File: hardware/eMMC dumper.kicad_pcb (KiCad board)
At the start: 2 copper layers, 85.8 x 55 mm, 49 parts, among them U1 F1C100s, U2 AMS1117-3.3, U3 TLV75512PDBV (WL9193S5-12), U4 EMMC04G-M627-A01

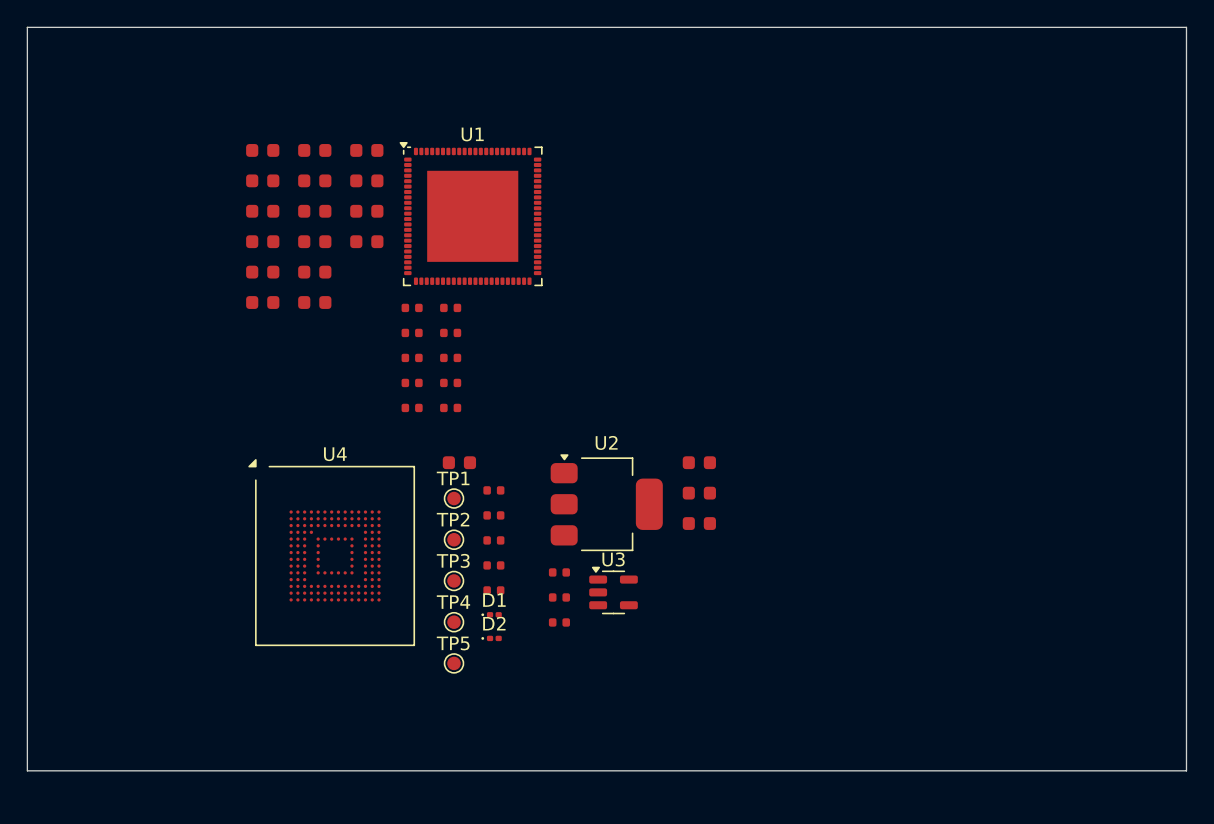
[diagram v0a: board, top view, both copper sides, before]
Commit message: Started placing decoupling capacitors
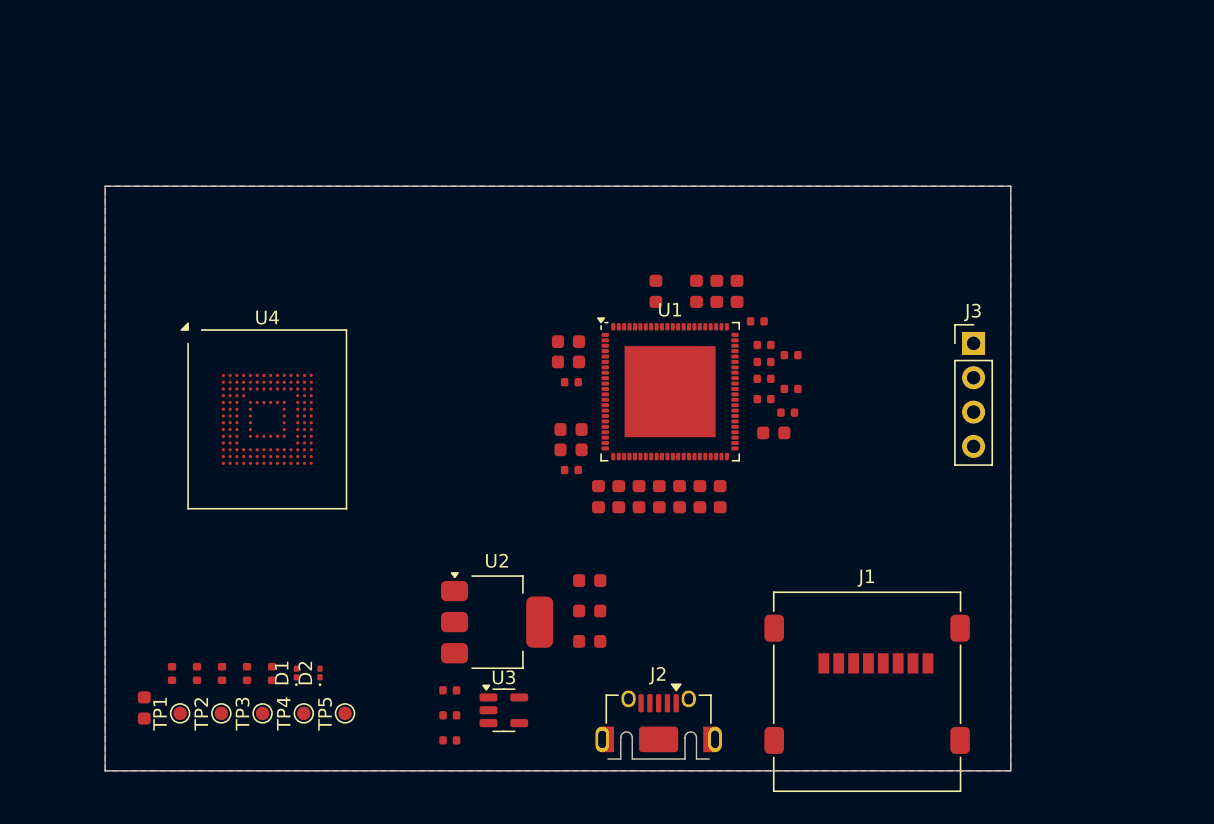
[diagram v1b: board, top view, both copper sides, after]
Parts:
- added J1: Micro_SD_Card, Connector_Card:microSD_HC_Molex_47219-2001, F.Cu at (182.1, 119.4)
- added J2: USB_B_Micro, Connector_USB:USB_Micro-AB_Molex_47590-0001, F.Cu at (166.7, 123.3)
- added J3: Conn_01x04, Connector_PinHeader_2.54mm:PinHeader_1x04_P2.54mm_Vertical, F.Cu at (190.0, 93.6)
- moved C9 39.9 mm to (169.8, 105.0), turned to -90 degrees
- moved C13 39.0 mm to (175.2, 100.2)
- moved C16 36.7 mm to (171.2, 105.0), turned to -90 degrees
- moved C11 35.3 mm to (172.5, 89.8), turned to 90 degrees
- moved C10 34.1 mm to (171.0, 89.8), turned to 90 degrees
- moved C18 32.9 mm to (168.2, 105.0), turned to -90 degrees
- moved C7 31.8 mm to (160.2, 101.5), turned to 180 degrees
- moved C19 30.4 mm to (166.8, 105.0), turned to -90 degrees
- moved C26 29.5 mm to (128.7, 120.6), turned to 90 degrees
- moved C23 28.2 mm to (163.8, 105.0), turned to -90 degrees
- moved R1 28.1 mm to (176.5, 94.5), turned to 180 degrees
- moved C24 27.6 mm to (165.2, 105.0), turned to -90 degrees
- moved R8 27.4 mm to (130.7, 118.0), turned to 90 degrees
- moved C14 27.3 mm to (166.5, 89.8), turned to 90 degrees
- moved C21 26.5 mm to (169.5, 89.8), turned to 90 degrees
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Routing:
- added copper zone on B.Cu, net GND
- added copper zone on F.Cu, net GND
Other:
- board size 85.8 x 55 mm -> 67 x 43.2 mm

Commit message: PCB major changes
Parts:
- removed J3: Conn_01x04, Connector_PinHeader_2.54mm:PinHeader_1x04_P2.54mm_Vertical
- added D3: LED, LED_SMD:LED_0201_0603Metric, F.Cu at (182.5, 93.6)
- added D4: LED, LED_SMD:LED_0201_0603Metric, F.Cu at (185.8, 93.6)
- added D5: LED, LED_SMD:LED_0201_0603Metric, F.Cu at (164.0, 116.4)
- added H1: MountingHole, MountingHole:MountingHole_3.2mm_M3, F.Cu at (128.8, 120.6)
- added H2: MountingHole, MountingHole:MountingHole_3.2mm_M3, F.Cu at (190.4, 95.8)
- added R13: 1kΩ, PCM_JLCPCB:R_0603, F.Cu at (177.0, 96.4)
- added R14: 1kΩ, PCM_JLCPCB:R_0603, F.Cu at (179.2, 96.4)
- added R15: 1kΩ, PCM_JLCPCB:R_0603, F.Cu at (181.5, 96.4)
- added R16: 1kΩ, PCM_JLCPCB:R_0603, F.Cu at (183.8, 96.4)
- added R17: 1kΩ, PCM_JLCPCB:R_0603, F.Cu at (160.2, 116.4)
- added TP6: TestPoint, TestPoint:TestPoint_Pad_D1.0mm, F.Cu at (149.2, 112.6)
- added TP7: TestPoint, TestPoint:TestPoint_Pad_D1.0mm, F.Cu at (153.4, 112.6)
- added TP8: TestPoint, TestPoint:TestPoint_Pad_D1.0mm, F.Cu at (157.8, 112.8)
- moved C26 54.8 mm to (182.6, 110.6), turned to 0 degrees
- moved D2 44.9 mm to (179.2, 93.5)
- moved TP1 44.5 mm to (171.2, 101.4)
- moved D1 43.5 mm to (175.8, 93.4)
- moved TP2 42.9 mm to (171.2, 99.0)
- moved TP3 41.8 mm to (171.2, 96.4)
- moved R8 39.8 mm to (170.1, 112.6), turned to 0 degrees
- moved R9 38.1 mm to (170.1, 111.6), turned to 0 degrees
- moved R10 36.5 mm to (170.1, 110.6), turned to 0 degrees
- moved R11 34.9 mm to (170.1, 109.6), turned to 0 degrees
- moved R12 33.4 mm to (170.1, 108.6), turned to 0 degrees
- moved C10 27.3 mm to (144.9, 97.8)
- moved C11 27.3 mm to (146.4, 97.8)
- moved C12 27.3 mm to (134.2, 108.0)
- moved C13 27.3 mm to (149.2, 108.3)
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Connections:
- D1 pad 2: /Linux_core/LED_GRN -> /Linux_core/LED_1
- D2 pad 2: /Linux_core/LED_RED -> /Linux_core/LED_2
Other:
- board size 67 x 43.2 mm -> 69.4 x 36 mm
- board text added: "0x01 init"
- board text added: "0x02 boot1"
- board text added: "0x03 boot2"
- board text added: "0x04 usrsp"
- board text added: "0x05 gmem"
- board text added: "0x06 bmem"
- board text added: "0x07 finish"
- board text added: "0x08 error"

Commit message: Moved LEDs, renamed testpoints
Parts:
- moved D4 58.9 mm to (126.9, 95.6), turned to -90 degrees
- moved R16 57.4 mm to (126.9, 104.3), turned to -90 degrees
- moved D3 53.8 mm to (128.7, 95.5), turned to -90 degrees
- moved R15 53.1 mm to (128.7, 102.3), turned to -90 degrees
- moved R14 49.0 mm to (130.4, 100.5), turned to -90 degrees
- moved D2 48.7 mm to (130.5, 95.5), turned to -90 degrees
- moved R13 44.6 mm to (132.5, 99.0), turned to -90 degrees
- moved D1 43.4 mm to (132.4, 95.5), turned to -90 degrees
- moved H2 24.5 mm to (190.1, 120.3)
- moved R12 10.8 mm to (180.8, 110.1)
- moved R11 9.95 mm to (179.9, 111.3)
- moved C26 7.77 mm to (186.0, 117.6), turned to 90 degrees
- moved R10 5.26 mm to (175.3, 111.4)
- moved J1 5.03 mm to (177.1, 119.5)
- moved R9 3.92 mm to (173.8, 110.3)
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- renumbered TP5 to 1V2, TP4 to 3V3, TP2 to CLK1, TP1 to CMD1, TP3 to D0, TP8 to GND1, TP7 to U_RX1, TP6 to U_TX1
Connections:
- R13 pad 2: unconnected-(R13-Pad2) -> Net-(U1A-PD0/LCD_D2/TWI0_SDA/RSB_SDA/EINTD0)
- R14 pad 2: unconnected-(R14-Pad2) -> Net-(U1A-PD1/LCD_D3/UART1_RTS/EINTD1)
- R15 pad 2: unconnected-(R15-Pad2) -> Net-(U1A-PD2/LCD_D4/UART1_CTS/EINTD2)
- R16 pad 2: unconnected-(R16-Pad2) -> Net-(U1A-PD3/LCD_D5/UART1_RX/EINTD3)
- U1 pad 6: unconnected-(U1A-PD0/LCD_D2/TWI0_SDA/RSB_SDA/EINTD0-Pad6) -> Net-(U1A-PD0/LCD_D2/TWI0_SDA/RSB_SDA/EINTD0)
- U1 pad 7: unconnected-(U1A-PD1/LCD_D3/UART1_RTS/EINTD1-Pad7) -> Net-(U1A-PD1/LCD_D3/UART1_RTS/EINTD1)
- U1 pad 8: unconnected-(U1A-PD2/LCD_D4/UART1_CTS/EINTD2-Pad8) -> Net-(U1A-PD2/LCD_D4/UART1_CTS/EINTD2)
- U1 pad 9: unconnected-(U1A-PD3/LCD_D5/UART1_RX/EINTD3-Pad9) -> Net-(U1A-PD3/LCD_D5/UART1_RX/EINTD3)
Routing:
- net +3V3: track 0.00 -> 11.8 mm
- net GND: track 0.00 -> 8.96 mm
- net /Linux_core/D3: track 0.00 -> 7.50 mm
- net /Linux_core/D1: track 0.00 -> 7.43 mm
- net /Linux_core/D2: track 0.00 -> 6.29 mm
- net /Linux_core/D0: track 0.00 -> 6.23 mm
- net /Linux_core/CMD: track 0.00 -> 6.12 mm

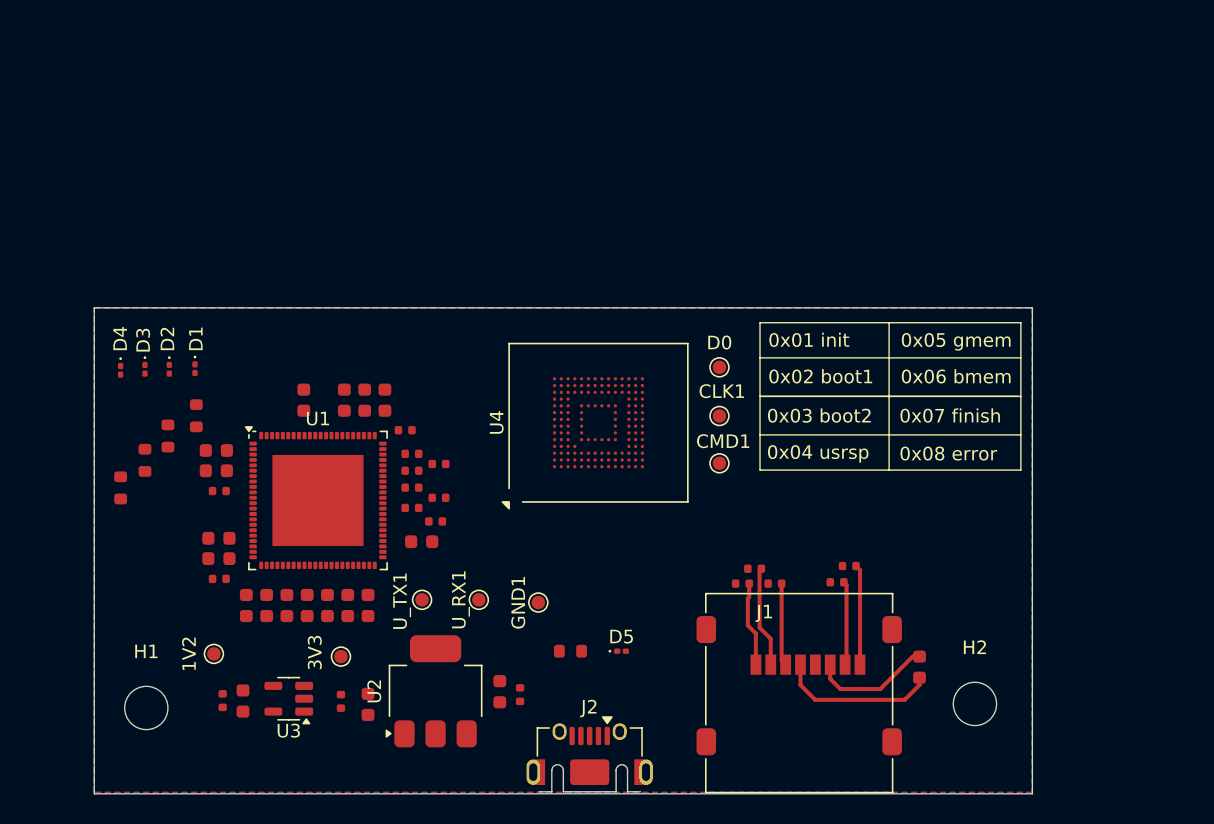
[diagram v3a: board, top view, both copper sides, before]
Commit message: Moved some parts, started routing
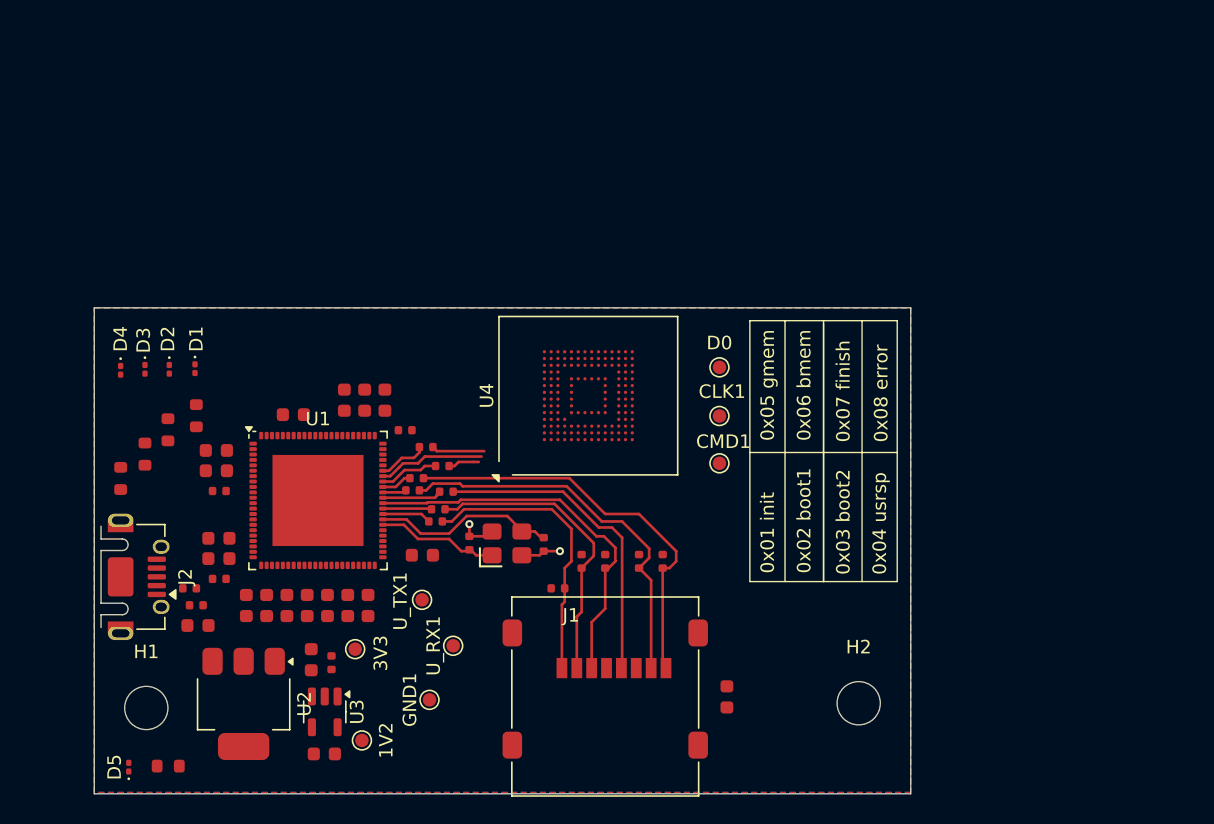
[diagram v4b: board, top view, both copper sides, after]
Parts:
- added C27: 18pF, PCM_JLCPCB:C_0402, F.Cu at (152.7, 108.4)
- added C28: 18pF, PCM_JLCPCB:C_0402, F.Cu at (158.2, 108.5)
- added X1: 24MHz, PCM_JLCPCB:OSC-SMD_4P-L3.2-W2.5-BL, F.Cu at (155.5, 108.4)
- moved J2 38.0 mm to (126.5, 110.9), turned to -90 degrees
- moved D5 37.5 mm to (127.5, 125.0), turned to 90 degrees
- moved R17 31.0 mm to (130.4, 124.9), turned to 0 degrees
- moved C5 24.8 mm to (132.5, 113.0), turned to 0 degrees
- moved C1 22.9 mm to (132.6, 114.5), turned to 0 degrees
- moved R11 14.7 mm to (165.2, 109.8), turned to -90 degrees
- moved C26 14.4 mm to (171.8, 119.8)
- moved J1 14.4 mm to (162.8, 119.8)
- moved U2 14.2 mm to (136.0, 120.3), turned to -90 degrees
- moved R12 13.8 mm to (167.0, 109.8), turned to -90 degrees
- moved R8 13.7 mm to (159.2, 111.8)
- moved R9 12.8 mm to (161.0, 109.8), turned to -90 degrees
- moved 1V2 12.7 mm to (144.8, 123.0), turned to -90 degrees
- moved R10 12.7 mm to (162.8, 109.8), turned to -90 degrees
- moved GND1 10.8 mm to (149.8, 120.0)
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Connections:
- U1 pad 51: unconnected-(U1A-HOSCI-Pad51) -> Net-(U1A-HOSCI)
- U1 pad 52: unconnected-(U1A-HOSCO-Pad52) -> Net-(U1A-HOSCO)
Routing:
- net /Linux_core/CLK: track 0.00 -> 23.6 mm
- net /Linux_core/D1: track 7.43 -> 30.4 mm
- net /Linux_core/D0: track 6.23 -> 28.7 mm
- net /Linux_core/CMD: track 6.12 -> 28.5 mm
- net /Linux_core/D2: track 6.29 -> 21.1 mm
- net /Linux_core/D3: track 7.50 -> 22.1 mm
- net Net-(U1A-HOSCO): track 0.00 -> 13.6 mm
- net +3V3: track 11.8 -> 0.00 mm
- net Net-(U1A-HOSCI): track 0.00 -> 9.10 mm
- net /Linux_core/CMD_eMMC: track 0.00 -> 7.90 mm
- net Net-(U1A-PF2/SDC0_CLK/UART0_RX/EINTF2): track 0.00 -> 4.44 mm
- net Net-(U1A-PC0/SPI0_CLK/SDC1_CLK): track 0.00 -> 4.38 mm
- net /Linux_core/D0_eMMC: track 0.00 -> 3.92 mm
- net Net-(U1A-PC2/SPI0_MISO/SDC1_D0): track 0.00 -> 3.66 mm
- net Net-(U1A-PF5/SDC0_D2/DBG_CK/PWM1/EINTF5): track 0.00 -> 3.63 mm
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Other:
- board size 69.4 x 36 mm -> 60.4 x 36 mm
